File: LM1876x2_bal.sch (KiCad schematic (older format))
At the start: 38 parts, among them J1 INPUT, J10 STBY, J11 V+, J2 OUTPUT, J3 POWER, J4 Conn_01x01_Male, J5 Conn_01x01_Male, J6 Conn_01x01_Male, J7 Conn_01x01_Male, J8 Conn_01x01_Male, J9 MUTE, U1 LM1876

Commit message: added imgs
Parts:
- J4: value Conn_01x01_Male -> SPK
- J5, J7: value Conn_01x01_Male -> GND
- J6: value Conn_01x01_Male -> VEE
- J8: value Conn_01x01_Male -> VCC
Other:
- moved on the sheet: J3, J4, J5, J6, J7, J8
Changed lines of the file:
@@
 L Connector:Screw_Terminal_01x03 J3
 U 1 1 645E988E
-P 7550 4700
-F 0 "J3" H 7630 4742 50  0000 L CNN
-F 1 "POWER" H 7630 4651 50  0000 L CNN
-F 2 "local_lib_footprints:TerminalBlock_CUI_01x03_P5.00mm" H 7550 4700 50  0001 C CNN
-F 3 "~" H 7550 4700 50  0001 C CNN
-	1    7550 4700
+P 7550 4400
+F 0 "J3" H 7630 4442 50  0000 L CNN
+F 1 "POWER" H 7630 4351 50  0000 L CNN
+F 2 "local_lib_footprints:TerminalBlock_CUI_01x03_P5.00mm" H 7550 4400 50  0001 C CNN
+F 3 "~" H 7550 4400 50  0001 C CNN
+	1    7550 4400
 	1    0    0    -1
 $EndComp
@@
 L power:VEE #PWR016
 U 1 1 645EB771
-P 7250 4600
-F 0 "#PWR016" H 7250 4450 50  0001 C CNN
-F 1 "VEE" V 7265 4727 50  0000 L CNN
-F 2 "" H 7250 4600 50  0001 C CNN
-F 3 "" H 7250 4600 50  0001 C CNN
-	1    7250 4600
+P 7250 4300
+F 0 "#PWR016" H 7250 4150 50  0001 C CNN
+F 1 "VEE" V 7265 4427 50  0000 L CNN
+F 2 "" H 7250 4300 50  0001 C CNN
+F 3 "" H 7250 4300 50  0001 C CNN
+	1    7250 4300
 	0    -1   -1   0
 $EndComp
@@
 L power:GND #PWR017
 U 1 1 645EBC39
-P 7250 4700
-F 0 "#PWR017" H 7250 4450 50  0001 C CNN
-F 1 "GND" V 7255 4572 50  0000 R CNN
-F 2 "" H 7250 4700 50  0001 C CNN
-F 3 "" H 7250 4700 50  0001 C CNN
-	1    7250 4700
+P 7250 4400
+F 0 "#PWR017" H 7250 4150 50  0001 C CNN
+F 1 "GND" V 7255 4272 50  0000 R CNN
+F 2 "" H 7250 4400 50  0001 C CNN
+F 3 "" H 7250 4400 50  0001 C CNN
+	1    7250 4400
 	0    1    1    0
 $EndComp
@@
 L power:VCC #PWR018
 U 1 1 645EBF10
-P 7250 4800
-F 0 "#PWR018" H 7250 4650 50  0001 C CNN
-F 1 "VCC" V 7265 4927 50  0000 L CNN
-F 2 "" H 7250 4800 50  0001 C CNN
-F 3 "" H 7250 4800 50  0001 C CNN
-	1    7250 4800
-	0    -1   -1   0
-$EndComp
-Wire Wire Line
-	7250 4600 7350 4600
-Wire Wire Line
-	7250 4700 7350 4700
-Wire Wire Line
-	7250 4800 7350 4800
+P 7250 4500
+F 0 "#PWR018" H 7250 4350 50  0001 C CNN
+F 1 "VCC" V 7265 4627 50  0000 L CNN
+F 2 "" H 7250 4500 50  0001 C CNN
+F 3 "" H 7250 4500 50  0001 C CNN
+	1    7250 4500
+	0    -1   -1   0
+$EndComp
+Wire Wire Line
+	7250 4300 7350 4300
+Wire Wire Line
+	7250 4400 7350 4400
+Wire Wire Line
+	7250 4500 7350 4500
 $Comp
 L power:GND #PWR010
@@
 L Connector:Conn_01x01_Male J4
 U 1 1 64596E7F
-P 7550 5200
-F 0 "J4" H 7522 5132 50  0000 R CNN
-F 1 "Conn_01x01_Male" H 7522 5223 50  0000 R CNN
-F 2 "local_lib_footprints:Terminal_.25_PCB_TAB_TE_Connectivity_P5.08mm_" H 7550 5200 50  0001 C CNN
-F 3 "~" H 7550 5200 50  0001 C CNN
-	1    7550 5200
+P 7550 4900
+F 0 "J4" H 7522 4832 50  0000 R CNN
+F 1 "SPK" H 7522 4923 50  0000 R CNN
+F 2 "local_lib_footprints:Terminal_.25_PCB_TAB_TE_Connectivity_P5.08mm_" H 7550 4900 50  0001 C CNN
+F 3 "~" H 7550 4900 50  0001 C CNN
+	1    7550 4900
 	-1   0    0    1
 $EndComp
@@
 L Connector:Conn_01x01_Male J5
 U 1 1 645980B5
+P 7550 5100
+F 0 "J5" H 7522 5032 50  0000 R CNN
+F 1 "GND" H 7522 5123 50  0000 R CNN
+F 2 "local_lib_footprints:Terminal_.25_PCB_TAB_TE_Connectivity_P5.08mm_" H 7550 5100 50  0001 C CNN
+F 3 "~" H 7550 5100 50  0001 C CNN
+	1    7550 5100
+	-1   0    0    1
+$EndComp
+$Comp
+L Connector:Conn_01x01_Male J6
+U 1 1 6459879F
 P 7550 5400
-F 0 "J5" H 7522 5332 50  0000 R CNN
-F 1 "Conn_01x01_Male" H 7522 5423 50  0000 R CNN
+F 0 "J6" H 7522 5332 50  0000 R CNN
+F 1 "VEE" H 7522 5423 50  0000 R CNN
 F 2 "local_lib_footprints:Terminal_.25_PCB_TAB_TE_Connectivity_P5.08mm_" H 7550 5400 50  0001 C CNN
 F 3 "~" H 7550 5400 50  0001 C CNN
@@
 $EndComp
 $Comp
-L Connector:Conn_01x01_Male J6
-U 1 1 6459879F
-P 7550 5700
-F 0 "J6" H 7522 5632 50  0000 R CNN
-F 1 "Conn_01x01_Male" H 7522 5723 50  0000 R CNN
-F 2 "local_lib_footprints:Terminal_.25_PCB_TAB_TE_Connectivity_P5.08mm_" H 7550 5700 50  0001 C CNN
-F 3 "~" H 7550 5700 50  0001 C CNN
-	1    7550 5700
-	-1   0    0    1
-$EndComp
-$Comp
 L Connector:Conn_01x01_Male J7
 U 1 1 64598BFE
-P 7550 5900
-F 0 "J7" H 7522 5832 50  0000 R CNN
-F 1 "Conn_01x01_Male" H 7522 5923 50  0000 R CNN
-F 2 "local_lib_footprints:Terminal_.25_PCB_TAB_TE_Connectivity_P5.08mm_" H 7550 5900 50  0001 C CNN
-F 3 "~" H 7550 5900 50  0001 C CNN
-	1    7550 5900
+P 7550 5600
+F 0 "J7" H 7522 5532 50  0000 R CNN
+F 1 "GND" H 7522 5623 50  0000 R CNN
+F 2 "local_lib_footprints:Terminal_.25_PCB_TAB_TE_Connectivity_P5.08mm_" H 7550 5600 50  0001 C CNN
+F 3 "~" H 7550 5600 50  0001 C CNN
+	1    7550 5600
 	-1   0    0    1
 $EndComp
@@
 L Connector:Conn_01x01_Male J8
 U 1 1 645990C6
-P 7550 6100
-F 0 "J8" H 7522 6032 50  0000 R CNN
-F 1 "Conn_01x01_Male" H 7522 6123 50  0000 R CNN
-F 2 "local_lib_footprints:Terminal_.25_PCB_TAB_TE_Connectivity_P5.08mm_" H 7550 6100 50  0001 C CNN
-F 3 "~" H 7550 6100 50  0001 C CNN
-	1    7550 6100
+P 7550 5800
+F 0 "J8" H 7522 5732 50  0000 R CNN
+F 1 "VCC" H 7522 5823 50  0000 R CNN
+F 2 "local_lib_footprints:Terminal_.25_PCB_TAB_TE_Connectivity_P5.08mm_" H 7550 5800 50  0001 C CNN
+F 3 "~" H 7550 5800 50  0001 C CNN
+	1    7550 5800
 	-1   0    0    1
 $EndComp
@@
 L power:VEE #PWR020
 U 1 1 64599525
-P 7350 5700
-F 0 "#PWR020" H 7350 5550 50  0001 C CNN
-F 1 "VEE" V 7365 5827 50  0000 L CNN
-F 2 "" H 7350 5700 50  0001 C CNN
-F 3 "" H 7350 5700 50  0001 C CNN
-	1    7350 5700
-	0    -1   -1   0
-$EndComp
-$Comp
-L power:GND #PWR021
-U 1 1 64599A8F
-P 7350 5900
-F 0 "#PWR021" H 7350 5650 50  0001 C CNN
-F 1 "GND" V 7355 5772 50  0000 R CNN
-F 2 "" H 7350 5900 50  0001 C CNN
-F 3 "" H 7350 5900 50  0001 C CNN
-	1    7350 5900
-	0    1    1    0
-$EndComp
-$Comp
-L power:VCC #PWR022
-U 1 1 64599F9C
-P 7350 6100
-F 0 "#PWR022" H 7350 5950 50  0001 C CNN
-F 1 "VCC" V 7365 6227 50  0000 L CNN
-F 2 "" H 7350 6100 50  0001 C CNN
-F 3 "" H 7350 6100 50  0001 C CNN
-	1    7350 6100
-	0    -1   -1   0
-$EndComp
-$Comp
-L power:GND #PWR019
-U 1 1 6459A503
 P 7350 5400
-F 0 "#PWR019" H 7350 5150 50  0001 C CNN
-F 1 "GND" V 7355 5272 50  0000 R CNN
+F 0 "#PWR020" H 7350 5250 50  0001 C CNN
+F 1 "VEE" V 7365 5527 50  0000 L CNN
 F 2 "" H 7350 5400 50  0001 C CNN
 F 3 "" H 7350 5400 50  0001 C CNN
 	1    7350 5400
+	0    -1   -1   0
+$EndComp
+$Comp
+L power:GND #PWR021
+U 1 1 64599A8F
+P 7350 5600
+F 0 "#PWR021" H 7350 5350 50  0001 C CNN
+F 1 "GND" V 7355 5472 50  0000 R CNN
+F 2 "" H 7350 5600 50  0001 C CNN
+F 3 "" H 7350 5600 50  0001 C CNN
+	1    7350 5600
+	0    1    1    0
+$EndComp
+$Comp
+L power:VCC #PWR022
+U 1 1 64599F9C
+P 7350 5800
+F 0 "#PWR022" H 7350 5650 50  0001 C CNN
+F 1 "VCC" V 7365 5927 50  0000 L CNN
+F 2 "" H 7350 5800 50  0001 C CNN
+F 3 "" H 7350 5800 50  0001 C CNN
+	1    7350 5800
+	0    -1   -1   0
+$EndComp
+$Comp
+L power:GND #PWR019
+U 1 1 6459A503
+P 7350 5100
+F 0 "#PWR019" H 7350 4850 50  0001 C CNN
+F 1 "GND" V 7355 4972 50  0000 R CNN
+F 2 "" H 7350 5100 50  0001 C CNN
+F 3 "" H 7350 5100 50  0001 C CNN
+	1    7350 5100
 	0    1    1    0
 $EndComp
@@
 Wire Wire Line
 	7250 3650 7050 3650
-Text GLabel 7350 5200 0    50   Input ~ 0
+Text GLabel 7350 4900 0    50   Input ~ 0
 SPK
 $Comp

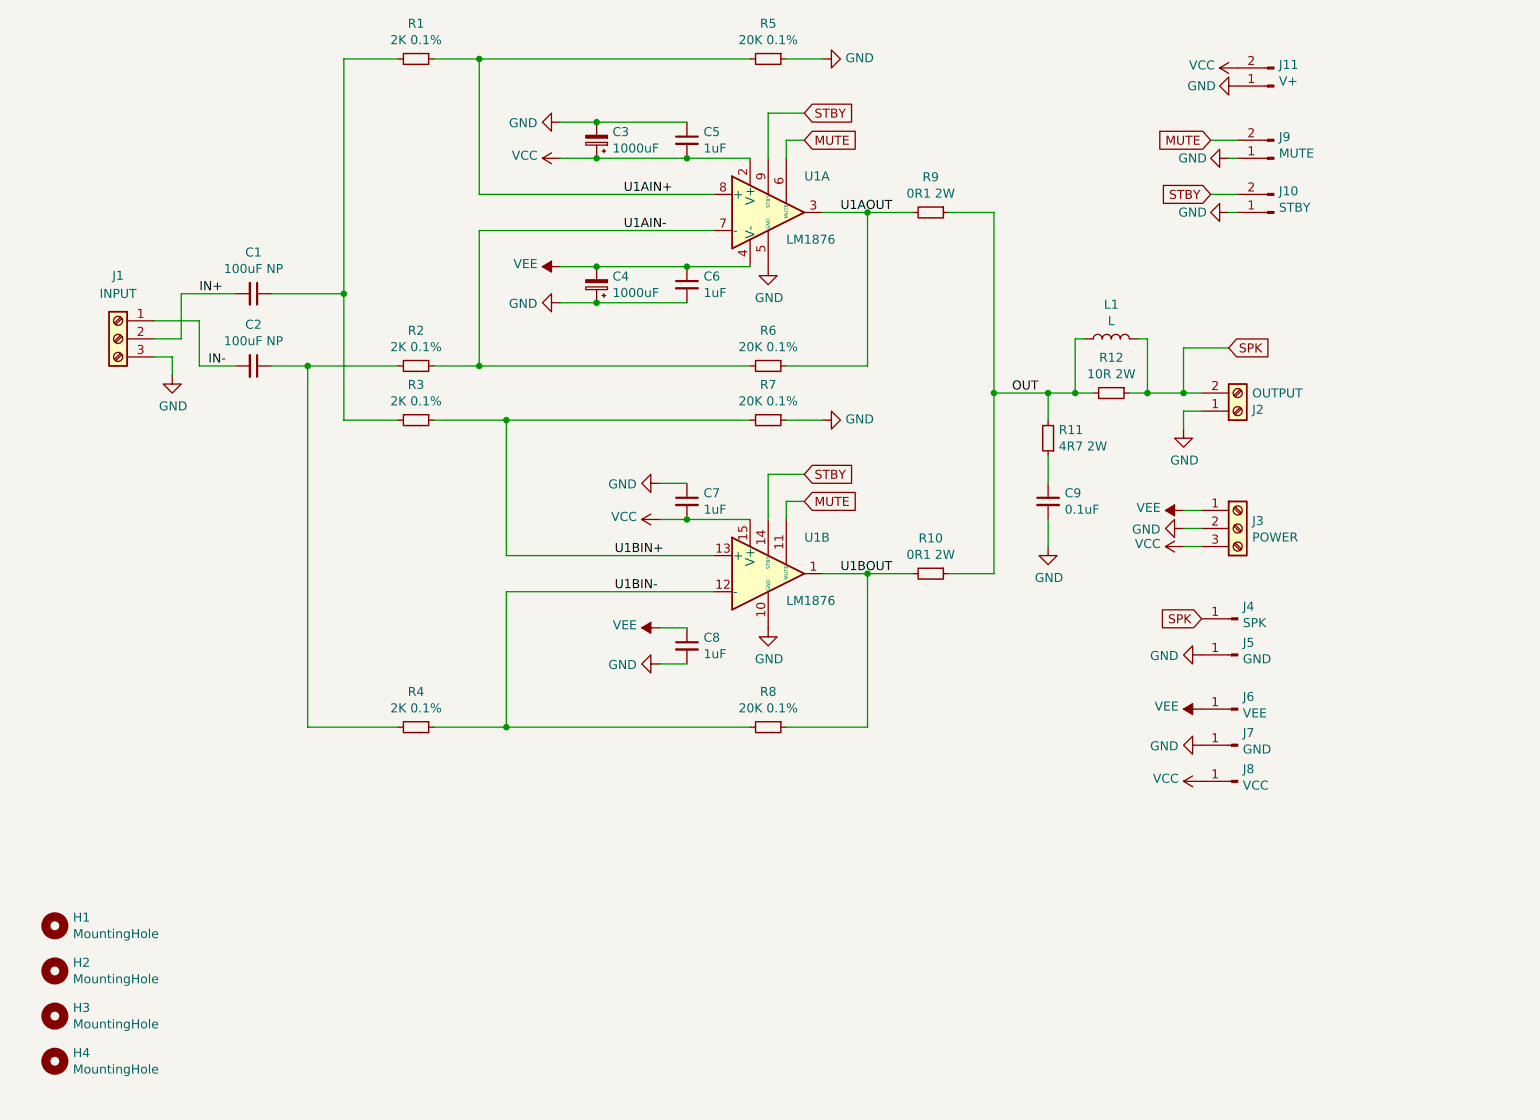
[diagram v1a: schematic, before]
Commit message: rev2.0 updates include adding mute delay circuit to the board
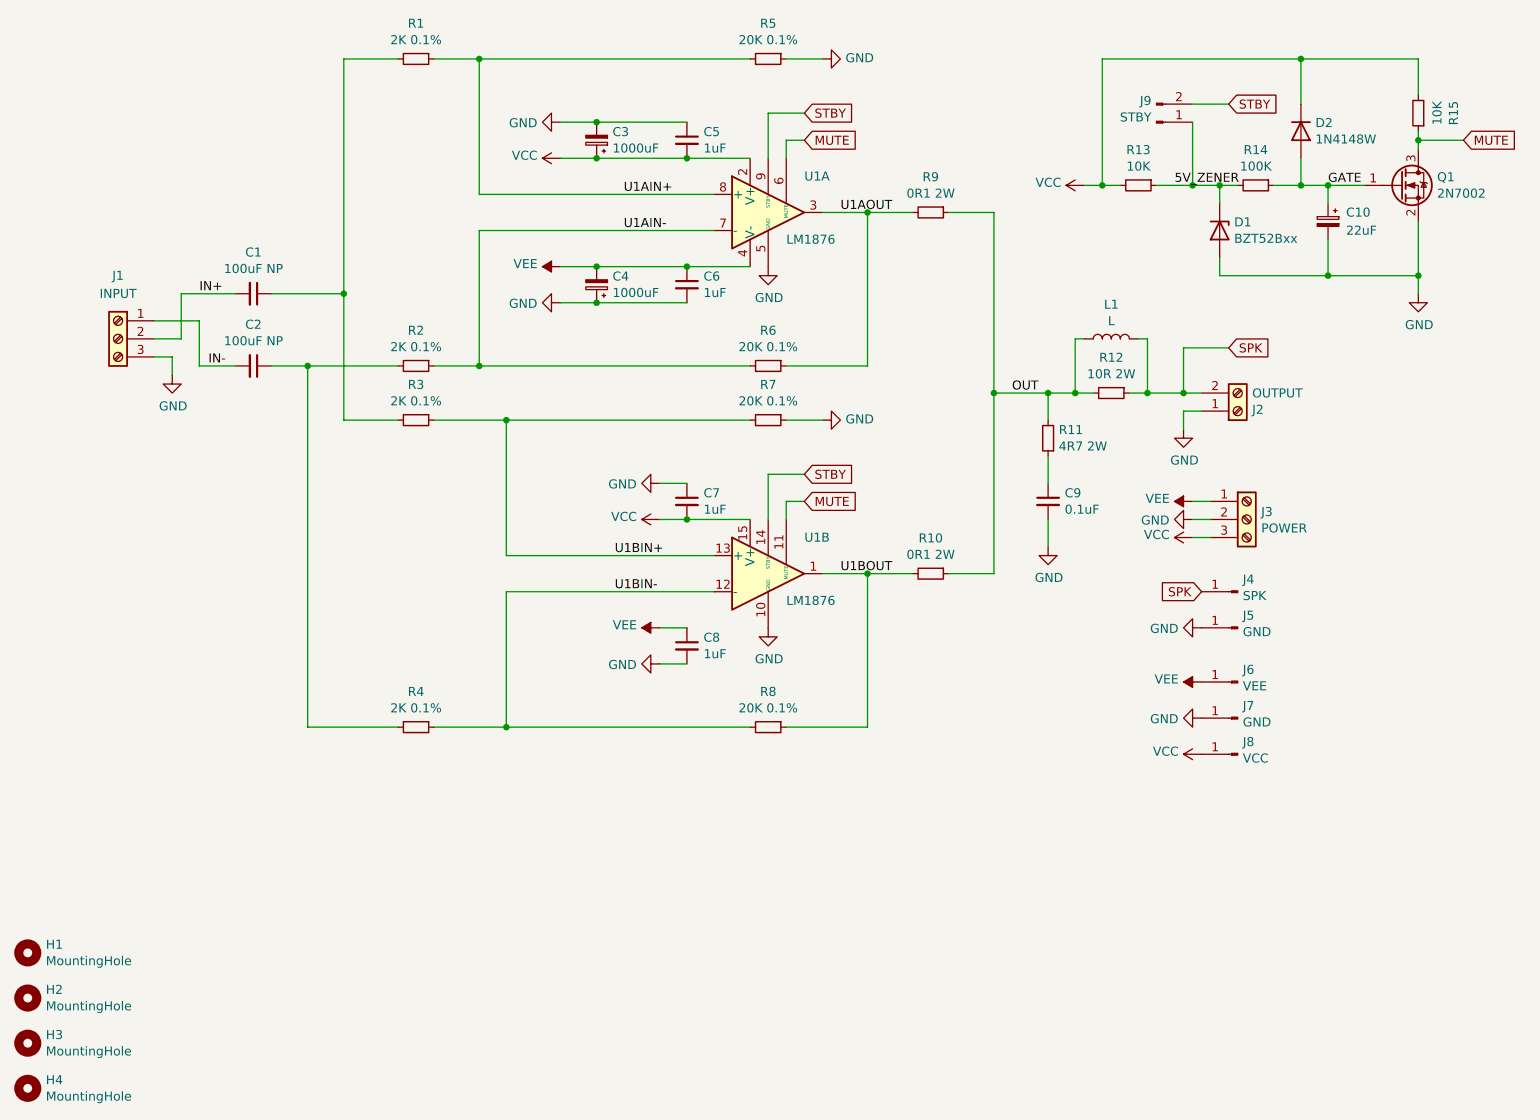
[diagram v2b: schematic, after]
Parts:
- removed J10: STBY, Connector_PinHeader_2.54mm:PinHeader_1x02_P2.54mm_Vertical, symbol Connector:Conn_01x02_Male
- removed J11: V+, Connector_PinHeader_2.54mm:PinHeader_1x02_P2.54mm_Vertical, symbol Connector:Conn_01x02_Male
- added C10: 22uF, Capacitor_THT:CP_Radial_D6.3mm_P2.50mm, symbol Device:CP_Small
- added D1: BZT52Bxx, Diode_SMD:D_SOD-123, symbol Diode:BZT52Bxx
- added D2: 1N4148W, Diode_SMD:D_SOD-123, symbol Diode:1N4148W
- added Q1: 2N7002, Package_TO_SOT_SMD:SOT-23, symbol Transistor_FET:2N7002
- added R13, R15: 10K, Resistor_SMD:R_1206_3216Metric_Pad1.42x1.75mm_HandSolder, symbol Device:R_Small
- added R14: 100K, Resistor_SMD:R_1206_3216Metric_Pad1.42x1.75mm_HandSolder, symbol Device:R_Small
- J9: value MUTE -> STBY
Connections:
- net GND: now also C10.2, D1.2 (A), Q1.2 (S); no longer J9.1 (Pin_1)
- net MUTE: now also Q1.3 (D), R15.1; no longer J9.2 (Pin_2)
- net STBY: now also J9.2 (Pin_2)
- net VCC: now also D2.1 (K), R13.2, R15.2
- new net 5V_ZENER: D1.1 (K), J9.1 (Pin_1), R13.1, R14.2
- new net GATE: C10.1, D2.2 (A), Q1.1 (G), R14.1
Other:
- moved on the sheet: H1, H2, H3, H4, J3, J4, J5, J6, J7, J8
